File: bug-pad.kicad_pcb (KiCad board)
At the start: 2 copper layers, 117.5 x 80 mm, 15 parts, among them SW1 SW_Push, SW2 SW_Push, SW3 SW_Push, SW4 SW_Push, SW5 RotaryEncoder_Switch, U1 MOUDLE-SEEEDUINO-XIAO, U2 ER_OLEDM0.91_1x-I2C

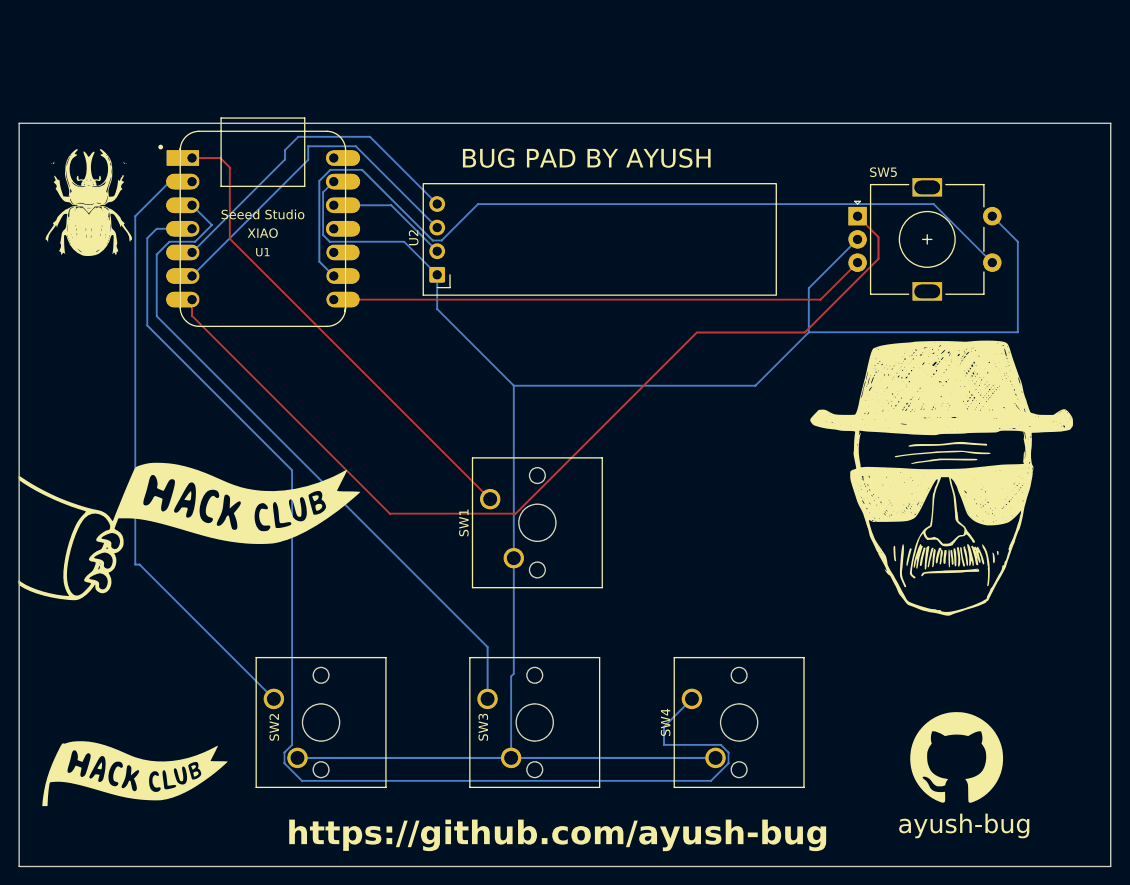
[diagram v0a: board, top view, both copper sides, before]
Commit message: change the design and size of pcb
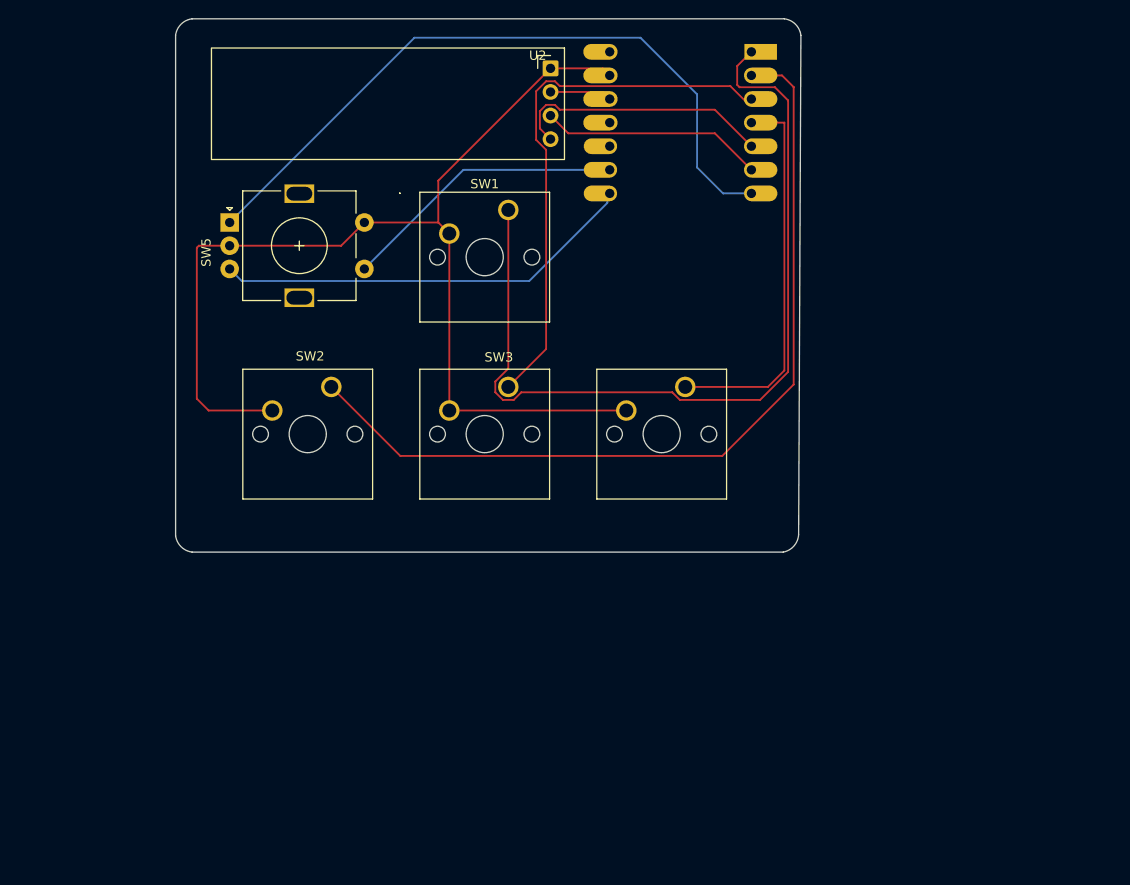
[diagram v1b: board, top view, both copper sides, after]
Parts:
- removed G***: LOGO, demo.preety:logo
- removed G***: LOGO, demo.preety:github-logo
- removed G***: LOGO, demo.preety:bug-pad-logo
- removed G***: LOGO, demo.preety:heisenberg
- removed G*** (x2): LOGO, demo.preety:hackclub-flag-left
- removed G***: LOGO, demo.preety:stardance-logo
- removed G***: LOGO, demo.preety:bug-butterfly
- U1: moved to B.Cu
- moved SW5 67.6 mm to (122.7, 85.7)
- moved U1 46.4 mm to (171.2, 74.9), turned to 180 degrees
- moved SW2 34.1 mm to (133.6, 103.4), turned to 0 degrees
- moved SW3 33.7 mm to (152.7, 103.4), turned to 0 degrees
- moved SW4 33.6 mm to (171.7, 103.4), turned to 0 degrees
- moved SW1 31.2 mm to (152.7, 84.3), turned to 0 degrees
- moved U2 25.4 mm to (157.2, 69.1), turned to -90 degrees
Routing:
- net Net-(U1-GND): track 248.3 -> 120.3 mm
- net Net-(U1-PA11_A3_D3): track 132.6 -> 41.6 mm
- net Net-(U1-PA7_A8_D8_SCK): track 91.2 -> 30.8 mm
- net Net-(U1-PA02_A0_D0): track 51.8 -> 93.6 mm
- net Net-(U1-PA4_A1_D1): track 66.1 -> 93.1 mm
- net Net-(U1-PB08_A6_D6_TX): track 101.3 -> 76.0 mm
- net Net-(U1-PA10_A2_D2): track 73.9 -> 61.1 mm
- net Net-(U1-PA9_A5_D5_SCL): track 36.7 -> 24.0 mm
- net Net-(U1-PB09_A7_D7_RX): track 58.0 -> 45.8 mm
- net Net-(U1-PA8_A4_D4_SDA): track 35.1 -> 28.4 mm
- net Net-(U1-3V3): track 13.2 -> 6.69 mm
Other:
- board size 117.5 x 80 mm -> 67.3 x 57.4 mm
- board text removed: "BUG PAD BY AYUSH"
- board text removed: "HACK CLUB"
- board text removed: "ayush-bug"
- board text removed: "https://github.com/ayush-bug"

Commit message: updated the gerber file
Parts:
- added G***: LOGO, demo.preety:github-logo, F.Cu at (171.2, 90.7)
- added G***: LOGO, demo.preety:bug-butterfly, B.Cu at (143.5, 72.6)
- added G***: LOGO, demo.preety:heisenberg, B.Cu at (125.7, 73.4)
- added G***: LOGO, demo.preety:stardance-logo, B.Cu at (150.4, 91.2)
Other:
- board text added: "BUGPAD by Ayush"
- board text added: "ayush-bug"
- board text added: "https://github.com/ayush-bug"
